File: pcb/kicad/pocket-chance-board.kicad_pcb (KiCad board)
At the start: 4 copper layers, 150 x 100 mm, 151 parts, among them J1 SWD, J2 USB4085-GF-A, J3 LiPo JST-PH 2.0mm (1 = + RED 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, J4 LCD 1.54in ST7789 module, JST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, J5 Speaker JST-PH, J6 microSD Molex 104031-0811, J7 STEMMA QT, J8 Expansion (6 = VBAT_SENSE ADC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, J9 LCD header 2.54 mm (wire by n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, Q1 FS8205A, Q3 AO3400A, Q4 AO3401A, Q6 AO3401A (DNP: fit only for a 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, SW1 BOOT, SW10 DPAD LEFT PTS645SM43SMTR92, SW11 DPAD RIGHT PTS645SM43SMTR92, SW12 DPAD PRESS PTS645SM43SMTR92, SW2 RESET, SW3 POWER PCM12, SW4 A PTS125SM43SMTR2LFS, SW5 B PTS125SM43SMTR2LFS, SW6 X PTS125SM43SMTR2LFS, SW7 Y PTS125SM43SMTR2LFS, SW8 DPAD UP PTS645SM43SMTR92, SW9 DPAD DOWN PTS645SM43SMTR92, U1 RP2350A, U10 LSM6DSOXTR, U11 RM2, U2 W25Q128JVSIQ, U3 APS6404L-3SQR-SN, U4 USBLC6-2SC6, U5 BQ24074RGTR, U6 TPS63001DRCR, U7 DW01A, U8 PAM8302AADCR, U9 DS3231MZ+, Y1 12MHz ABM8-272-T3

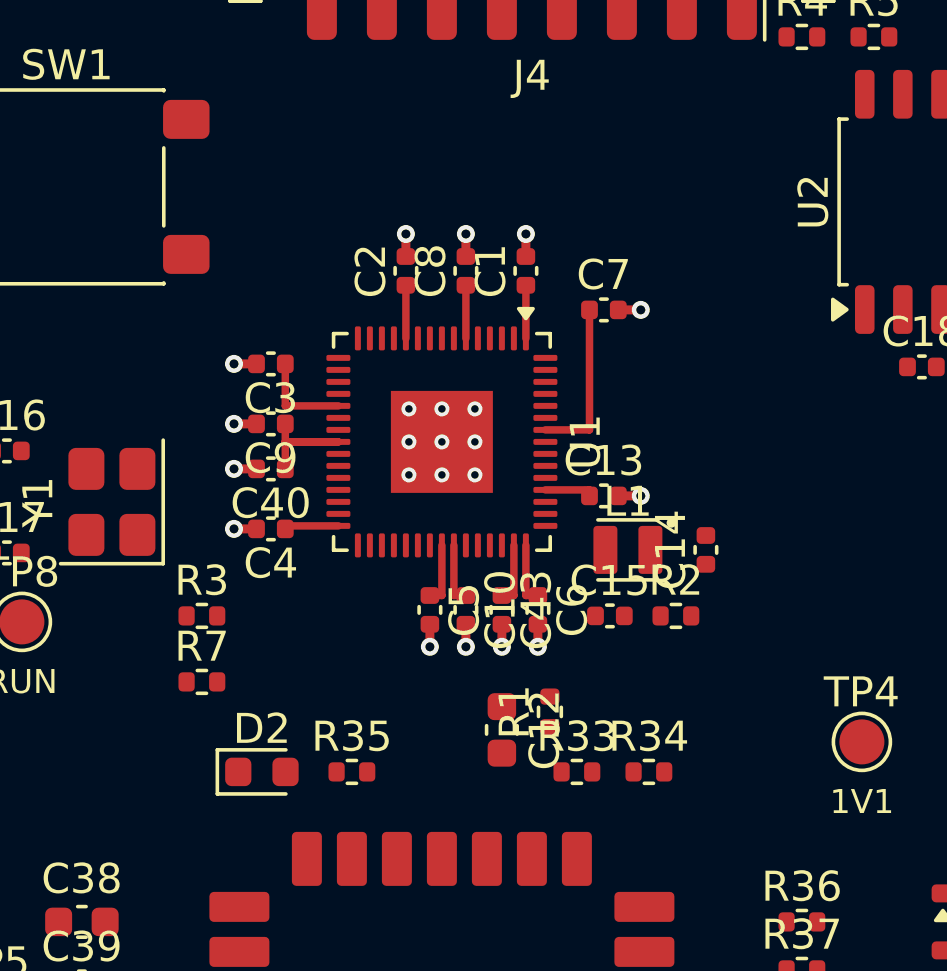
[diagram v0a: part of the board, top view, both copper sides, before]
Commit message: Layout: RP2350 decoupling ring moved to about 3.5 mm, each cap in its own pin's escape lane, +3V3 plane vias (expert's conditions)
- top/left caps in their own lanes 1.5 mm further out; C40 in pin 23's lane; C7 straddles pins 53/54
- bottom-row caps (C5, C10, C6) below the busy row, autorouted; C9 shared on 1V1 beside C14 (accepted fallback)
- C43 stays in pin 44's lane, C12 behind it; core regulator loop (L1, C13, C14) unchanged
DRC: only the unrouted connections. Schematic unchanged (rev 0.13).
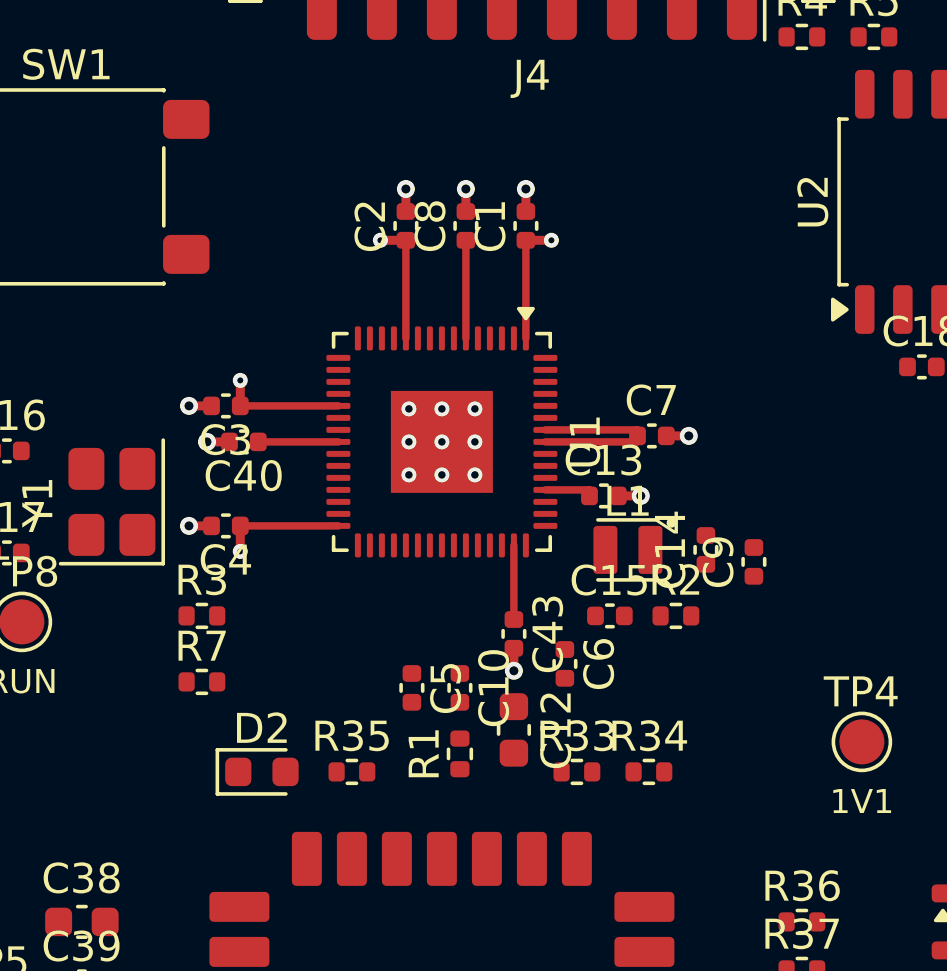
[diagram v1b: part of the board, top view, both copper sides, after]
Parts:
- moved C9 16.7 mm to (132.4, 124.0), turned to 90 degrees
- moved C7 4.49 mm to (129.0, 119.8)
- moved R1 3.31 mm to (122.6, 130.4)
- moved C5 2.67 mm to (121.0, 128.2)
- moved C10 2.61 mm to (122.6, 128.2)
- moved C3 2.05 mm to (114.8, 118.8)
- moved C6 2.01 mm to (126.1, 127.4)
- moved C4 1.50 mm to (114.8, 122.8)
- moved C1 1.50 mm to (124.8, 112.8)
- moved C2 1.50 mm to (120.8, 112.8)
- moved C8 1.50 mm to (122.8, 112.8)
- moved C40 1.27 mm to (115.4, 120.0)
- moved C43 0.89 mm to (124.4, 126.4)
- moved C12 0.40 mm to (124.4, 129.6)
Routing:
- net +3V3: track 19.9 -> 24.5 mm, vias 0 -> 4
- net GND: track 9.75 -> 6.75 mm, vias 22 -> 18
- net 1V1: track 8.88 -> 5.94 mm
